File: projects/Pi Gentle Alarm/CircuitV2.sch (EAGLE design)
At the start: 6 parts, among them IC1 7805T, X1 RASPI_BOARD_B+_E0, X2 22-23-2021

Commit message: Changed order sheet
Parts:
- F1: MF (none) -> RAYCHEM/POLYSWITCH; MPN (none) -> MINISMDC110F-2; OC_NEWARK (none) -> 98H4540
- IC1: MPN (none) -> NCP7805TG; OC_NEWARK (none) -> 81Y6957
- LED1, X1: OC_NEWARK (none) -> unknown
- Q1: MPN (none) -> 2N7000.; OC_NEWARK (none) -> 26AC6371
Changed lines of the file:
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@@
 <parts>
 <part name="FRAME1" library="frames" deviceset="A3L-LOC" device=""/>
-<part name="X1" library="raspberrypi_bastelstube_v13" deviceset="RASPI_BOARD_B+" device="_E0" value="RASPI_BOARD_B+_E0"/>
+<part name="X1" library="raspberrypi_bastelstube_v13" deviceset="RASPI_BOARD_B+" device="_E0" value="RASPI_BOARD_B+_E0">
+<attribute name="MF" value=""/>
+<attribute name="MPN" value=""/>
+<attribute name="OC_NEWARK" value="unknown"/>
+</part>
 <part name="X2" library="con-molex" library_urn="urn:adsk.eagle:library:165" deviceset="22-23-2021" device="" package3d_urn="urn:adsk.eagle:package:8078633/1"/>
-<part name="Q1" library="transistors" deviceset="2N700*" device="_TO92" technology="0"/>
+<part name="Q1" library="transistors" deviceset="2N700*" device="_TO92" technology="0">
+<attribute name="MF" value=""/>
+<attribute name="MPN" value="2N7000."/>
+<attribute name="OC_NEWARK" value="26AC6371"/>
+</part>
 <part name="P+1" library="supply1" library_urn="urn:adsk.eagle:library:371" deviceset="VCC" device=""/>
 <part name="GND1" library="supply1" library_urn="urn:adsk.eagle:library:371" deviceset="GND" device=""/>
-<part name="LED1" library="adafruit" library_urn="urn:adsk.eagle:library:420" deviceset="LED" device="SFH482" package3d_urn="urn:adsk.eagle:package:6240546/1"/>
-<part name="IC1" library="linear" library_urn="urn:adsk.eagle:library:262" deviceset="78*" device="T" package3d_urn="urn:adsk.eagle:package:16414/1" technology="05"/>
+<part name="LED1" library="adafruit" library_urn="urn:adsk.eagle:library:420" deviceset="LED" device="SFH482" package3d_urn="urn:adsk.eagle:package:6240546/1">
+<attribute name="MF" value=""/>
+<attribute name="MPN" value=""/>
+<attribute name="OC_NEWARK" value="unknown"/>
+</part>
+<part name="IC1" library="linear" library_urn="urn:adsk.eagle:library:262" deviceset="78*" device="T" package3d_urn="urn:adsk.eagle:package:16414/1" technology="05">
+<attribute name="MF" value=""/>
+<attribute name="MPN" value="NCP7805TG"/>
+<attribute name="OC_NEWARK" value="81Y6957"/>
+</part>
 <part name="P+2" library="supply1" library_urn="urn:adsk.eagle:library:371" deviceset="VCC" device=""/>
 <part name="GND2" library="supply1" library_urn="urn:adsk.eagle:library:371" deviceset="GND" device=""/>
-<part name="F1" library="MINISMDC110F-2" deviceset="MINISMDC110F-2" device=""/>
+<part name="F1" library="MINISMDC110F-2" deviceset="MINISMDC110F-2" device="">
+<attribute name="MF" value="RAYCHEM/POLYSWITCH"/>
+<attribute name="MPN" value="MINISMDC110F-2"/>
+<attribute name="OC_NEWARK" value="98H4540"/>
+</part>
 </parts>
 <sheets>
@@
 <attribute name="SHEET" x="357.505" y="5.08" size="2.54" layer="94"/>
 </instance>
-<instance part="X1" gate="G$1" x="88.9" y="154.94" smashed="yes"/>
+<instance part="X1" gate="G$1" x="88.9" y="154.94" smashed="yes">
+<attribute name="OC_NEWARK" x="88.9" y="154.94" size="1.778" layer="96" display="off"/>
+<attribute name="MF" x="88.9" y="154.94" size="1.778" layer="96" display="off"/>
+<attribute name="MPN" x="88.9" y="154.94" size="1.778" layer="96" display="off"/>
+</instance>
 <instance part="X2" gate="-1" x="119.38" y="198.12" smashed="yes">
 <attribute name="NAME" x="121.92" y="197.358" size="1.524" layer="95"/>
@@
 <attribute name="NAME" x="39.116" y="166.878" size="1.778" layer="95" rot="R180"/>
 <attribute name="VALUE" x="39.116" y="169.164" size="1.778" layer="96" rot="R180"/>
+<attribute name="OC_NEWARK" x="45.72" y="167.64" size="1.778" layer="96" display="off"/>
+<attribute name="MF" x="45.72" y="167.64" size="1.778" layer="96" display="off"/>
+<attribute name="MPN" x="45.72" y="167.64" size="1.778" layer="96" display="off"/>
 </instance>
 <instance part="P+1" gate="VCC" x="45.72" y="127" smashed="yes" rot="R180">
@@
 <attribute name="NAME" x="49.276" y="145.288" size="1.778" layer="95" rot="R90"/>
 <attribute name="VALUE" x="51.435" y="145.288" size="1.778" layer="96" rot="R90"/>
+<attribute name="OC_NEWARK" x="45.72" y="149.86" size="1.778" layer="96" display="off"/>
+<attribute name="MF" x="45.72" y="149.86" size="1.778" layer="96" display="off"/>
+<attribute name="MPN" x="45.72" y="149.86" size="1.778" layer="96" display="off"/>
 </instance>
 <instance part="IC1" gate="A1" x="83.82" y="226.06" smashed="yes" rot="R270">
 <attribute name="NAME" x="89.535" y="233.68" size="1.778" layer="95" rot="R270"/>
 <attribute name="VALUE" x="86.995" y="233.68" size="1.778" layer="96" rot="R270"/>
+<attribute name="OC_NEWARK" x="83.82" y="226.06" size="1.778" layer="96" display="off"/>
+<attribute name="MF" x="83.82" y="226.06" size="1.778" layer="96" display="off"/>
+<attribute name="MPN" x="83.82" y="226.06" size="1.778" layer="96" display="off"/>
 </instance>
 <instance part="P+2" gate="VCC" x="83.82" y="246.38" smashed="yes">
@@
 <attribute name="NAME" x="76.2" y="204.47" size="1.778" layer="95" rot="R90" align="center-left"/>
 <attribute name="VALUE" x="78.74" y="204.47" size="1.778" layer="96" rot="R90" align="center-left"/>
+<attribute name="OC_NEWARK" x="83.82" y="187.96" size="1.778" layer="96" display="off"/>
+<attribute name="MF" x="83.82" y="187.96" size="1.778" layer="96" display="off"/>
+<attribute name="MPN" x="83.82" y="187.96" size="1.778" layer="96" display="off"/>
 </instance>
 </instances>

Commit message: Finalization of the Alarm
Only steps are to post process and send
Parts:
- F1: value MINISMDC110F-2 -> (none); device MINISMDC110F-2:MINISMDC110F-2 -> Test:MF-MSMF260-2; MF RAYCHEM/POLYSWITCH -> (none); MPN MINISMDC110F-2 -> (none); OC_NEWARK 98H4540 -> (none)
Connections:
- net N$1: now also F1.P$1; no longer F1.1
- net N$2: now also F1.P$2; no longer F1.2
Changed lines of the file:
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@@
 <part name="P+2" library="supply1" library_urn="urn:adsk.eagle:library:371" deviceset="VCC" device=""/>
 <part name="GND2" library="supply1" library_urn="urn:adsk.eagle:library:371" deviceset="GND" device=""/>
-<part name="F1" library="MINISMDC110F-2" deviceset="MINISMDC110F-2" device="">
-<attribute name="MF" value="RAYCHEM/POLYSWITCH"/>
-<attribute name="MPN" value="MINISMDC110F-2"/>
-<attribute name="OC_NEWARK" value="98H4540"/>
-</part>
+<part name="F1" library="Test" deviceset="MF-MSMF260-2" device=""/>
 </parts>
 <sheets>
@@
 <attribute name="VALUE" x="60.96" y="228.6" size="1.778" layer="96" rot="R270"/>
 </instance>
-<instance part="F1" gate="G$1" x="83.82" y="187.96" smashed="yes" rot="R90">
-<attribute name="NAME" x="76.2" y="204.47" size="1.778" layer="95" rot="R90" align="center-left"/>
-<attribute name="VALUE" x="78.74" y="204.47" size="1.778" layer="96" rot="R90" align="center-left"/>
-<attribute name="OC_NEWARK" x="83.82" y="187.96" size="1.778" layer="96" display="off"/>
-<attribute name="MF" x="83.82" y="187.96" size="1.778" layer="96" display="off"/>
-<attribute name="MPN" x="83.82" y="187.96" size="1.778" layer="96" display="off"/>
-</instance>
+<instance part="F1" gate="G$1" x="83.82" y="200.66" smashed="yes" rot="R90"/>
 </instances>
 <busses>
@@
 <segment>
 <pinref part="X1" gate="G$1" pin="5V0"/>
-<pinref part="F1" gate="G$1" pin="1"/>
-<wire x1="83.82" y1="187.96" x2="83.82" y2="182.88" width="0.1524" layer="91"/>
+<wire x1="83.82" y1="187.96" x2="83.82" y2="192.66" width="0.1524" layer="91"/>
+<pinref part="F1" gate="G$1" pin="P$1"/>
+<wire x1="83.82" y1="192.66" x2="83.82" y2="182.88" width="0.1524" layer="91"/>
+<junction x="83.82" y="192.66"/>
 </segment>
 </net>
@@
 <segment>
 <pinref part="IC1" gate="A1" pin="VO"/>
-<pinref part="F1" gate="G$1" pin="2"/>
-<wire x1="83.82" y1="208.28" x2="83.82" y2="215.9" width="0.1524" layer="91"/>
+<wire x1="83.82" y1="208.28" x2="83.82" y2="208.66" width="0.1524" layer="91"/>
+<pinref part="F1" gate="G$1" pin="P$2"/>
+<wire x1="83.82" y1="208.66" x2="83.82" y2="215.9" width="0.1524" layer="91"/>
+<junction x="83.82" y="208.66"/>
 </segment>
 </net>

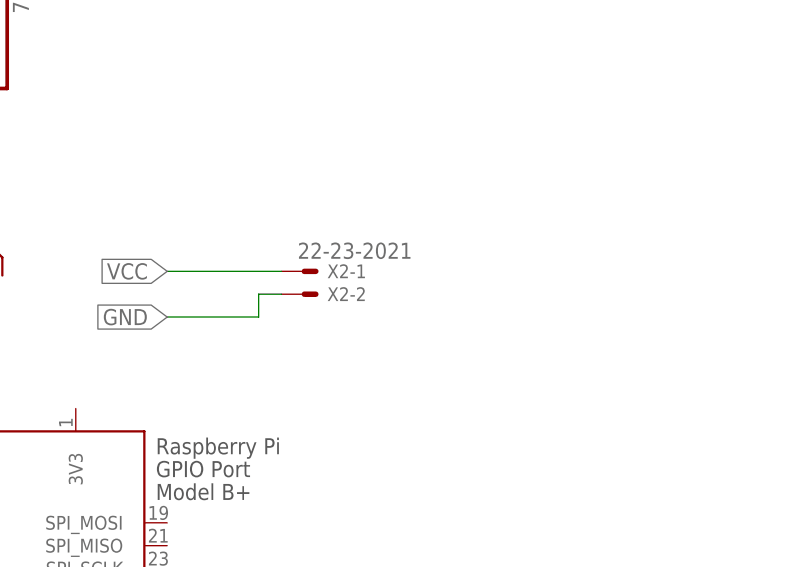
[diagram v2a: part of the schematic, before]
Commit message: Updated silkscreen
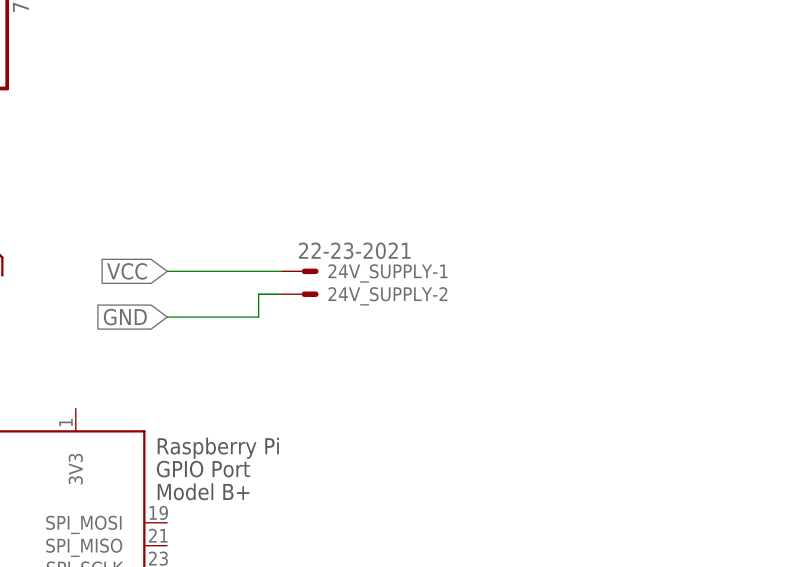
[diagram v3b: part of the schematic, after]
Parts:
- renumbered X2 to 24V_SUPPLY
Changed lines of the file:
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@@
 <attribute name="OC_NEWARK" value="unknown"/>
 </part>
-<part name="X2" library="con-molex" library_urn="urn:adsk.eagle:library:165" deviceset="22-23-2021" device="" package3d_urn="urn:adsk.eagle:package:8078633/1"/>
+<part name="24V_SUPPLY" library="con-molex" library_urn="urn:adsk.eagle:library:165" deviceset="22-23-2021" device="" package3d_urn="urn:adsk.eagle:package:8078633/1"/>
 <part name="Q1" library="transistors" deviceset="2N700*" device="_TO92" technology="0">
 <attribute name="MF" value=""/>
@@
 <attribute name="MPN" x="88.9" y="154.94" size="1.778" layer="96" display="off"/>
 </instance>
-<instance part="X2" gate="-1" x="119.38" y="198.12" smashed="yes">
+<instance part="24V_SUPPLY" gate="-1" x="119.38" y="198.12" smashed="yes">
 <attribute name="NAME" x="121.92" y="197.358" size="1.524" layer="95"/>
 <attribute name="VALUE" x="118.618" y="199.517" size="1.778" layer="96"/>
 </instance>
-<instance part="X2" gate="-2" x="119.38" y="195.58" smashed="yes">
+<instance part="24V_SUPPLY" gate="-2" x="119.38" y="195.58" smashed="yes">
 <attribute name="NAME" x="121.92" y="194.818" size="1.524" layer="95"/>
 </instance>
@@
 <net name="VCC" class="0">
 <segment>
-<pinref part="X2" gate="-1" pin="S"/>
+<pinref part="24V_SUPPLY" gate="-1" pin="S"/>
 <wire x1="116.84" y1="198.12" x2="104.14" y2="198.12" width="0.1524" layer="91"/>
 <label x="104.14" y="198.12" size="1.778" layer="95" rot="R180" xref="yes"/>
@@
 <net name="GND" class="0">
 <segment>
-<pinref part="X2" gate="-2" pin="S"/>
+<pinref part="24V_SUPPLY" gate="-2" pin="S"/>
 <wire x1="116.84" y1="195.58" x2="114.3" y2="195.58" width="0.1524" layer="91"/>
 <wire x1="114.3" y1="195.58" x2="114.3" y2="193.04" width="0.1524" layer="91"/>
